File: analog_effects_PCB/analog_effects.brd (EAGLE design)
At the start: 100 x 80 mm, 24 parts, among them J1 575-4, J2 575-4, U1 TL082

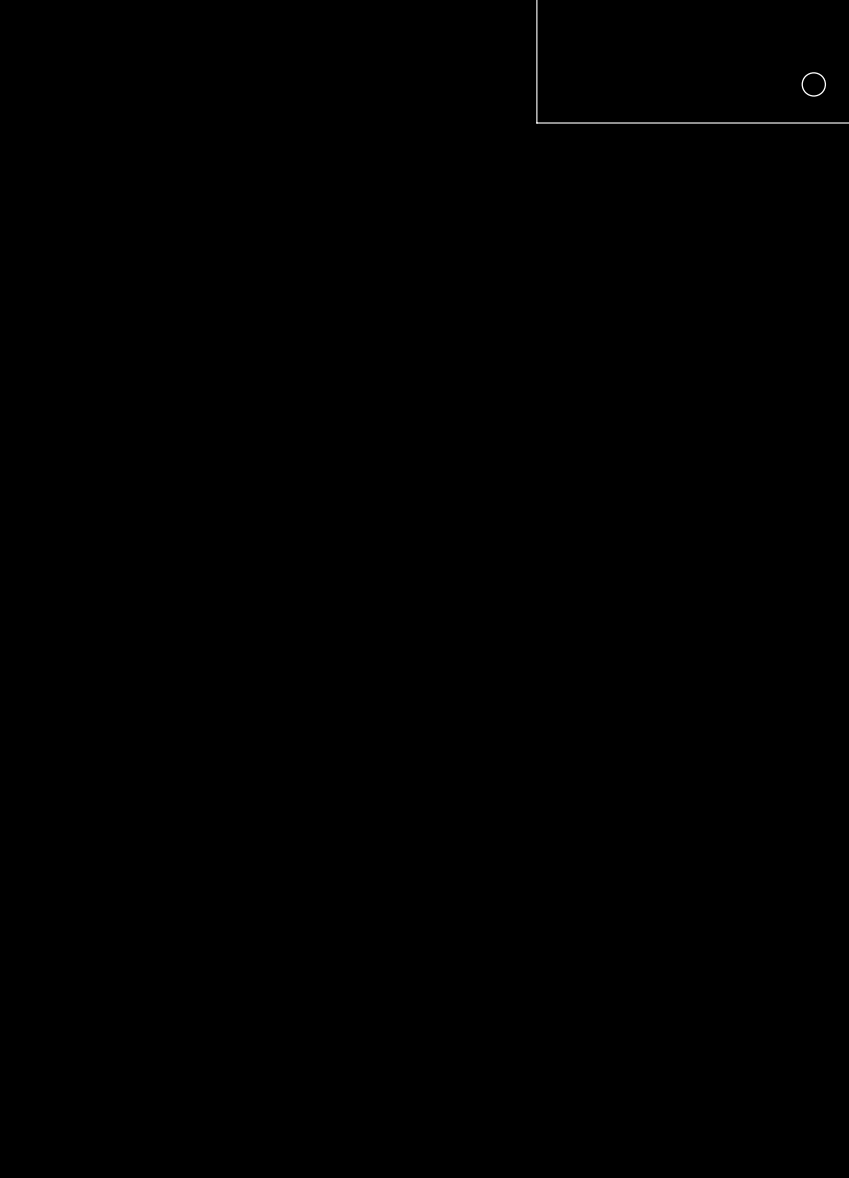
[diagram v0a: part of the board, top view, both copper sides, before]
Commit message: completed the digital pot circuitry on schematic
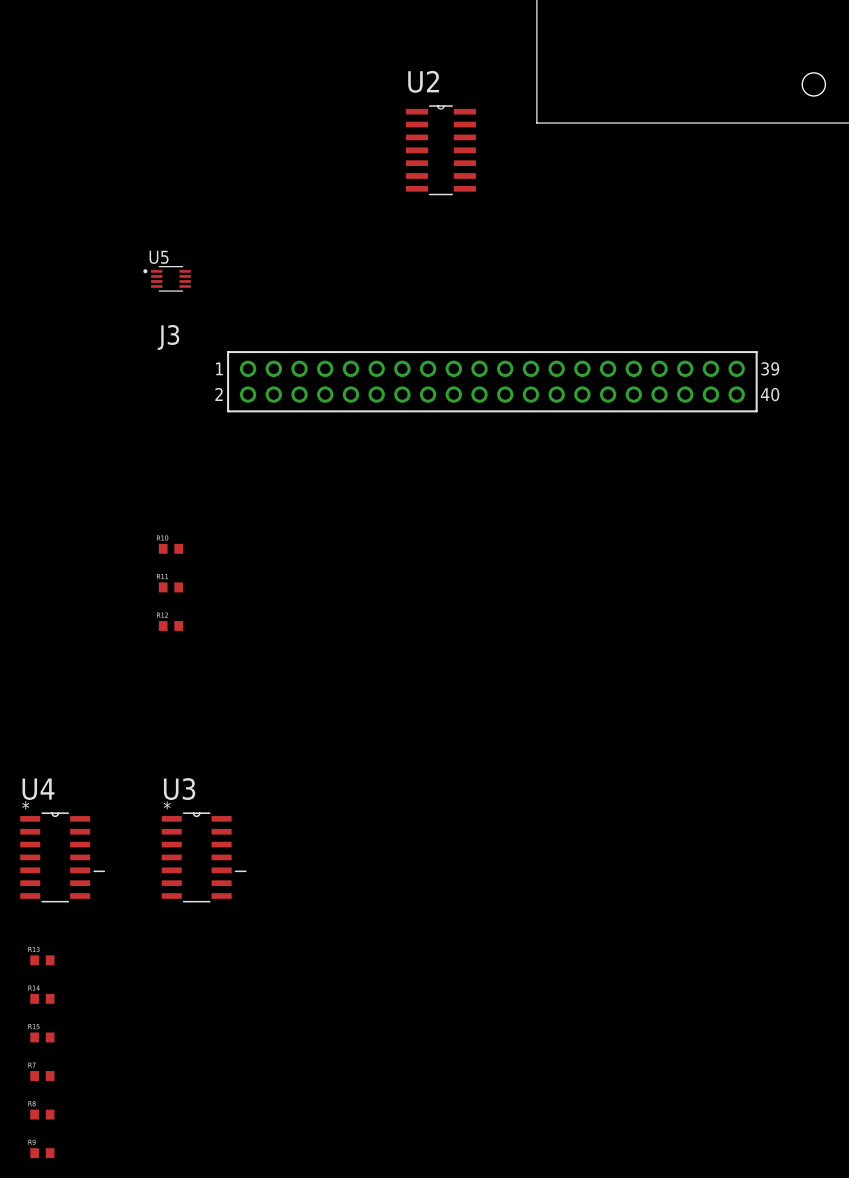
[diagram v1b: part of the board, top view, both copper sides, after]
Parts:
- added J3: SAMTEC-SSQ-120-01-X-DJ, SAMTEC-SSQ-120-01-X-D:SAMTEC-SSQ-120-01-X-D
- added R10, R11, R12, R13, R14, R15, R7, R8, R9: 100kΩ, CRCW0603100KDHEAP:RESC1508X50N
- added U2: AD5241BRZ1M, AD5241BRZ1M:SOIC127P600X175-14N
- added U3: AD5241BRZ10, AD5241BRZ10:SOIC127P600X175-14N
- added U4: AD5241BRZ100, AD5241BRZ100:SOIC127P600X175-14N
- added U5: TS5A3359DCUT, TS5A3359DCUT:SOP50P310X90-8N
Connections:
- new net N$12: R10.1, U2.5
- new net N$13: R3.2, TP6.1, U2.3
- new net N$14: R11.2, U2.7
- new net N$15: R10.2, R11.1, R12.2, U2.4
- new net N$16: C5.2, U3.3
- new net N$17: R12.1, U2.6
- new net N$19: R13.1, U4.7
- new net N$20: R13.2, R14.2, R15.2, U4.4
- new net N$21: R15.1, U4.6
- new net N$22: U3.2, U4.3
- new net N$23: R14.1, U4.5
- new net N$24: R7.1, U3.7
- new net N$25: R7.2, R8.2, R9.2, U3.4
- new net N$26: R9.1, U3.5
- new net N$27: R8.1, U3.6
- new net VCC: U5.8
- net GND: now also U2.10, U2.11, U2.8, U2.9, U3.10, U3.11, U3.8, U3.9, U4.10, U4.11, U4.2, U4.8, U4.9, U5.4; no longer C5.2
- net N$5: now also U2.2; no longer R3.2, TP6.1

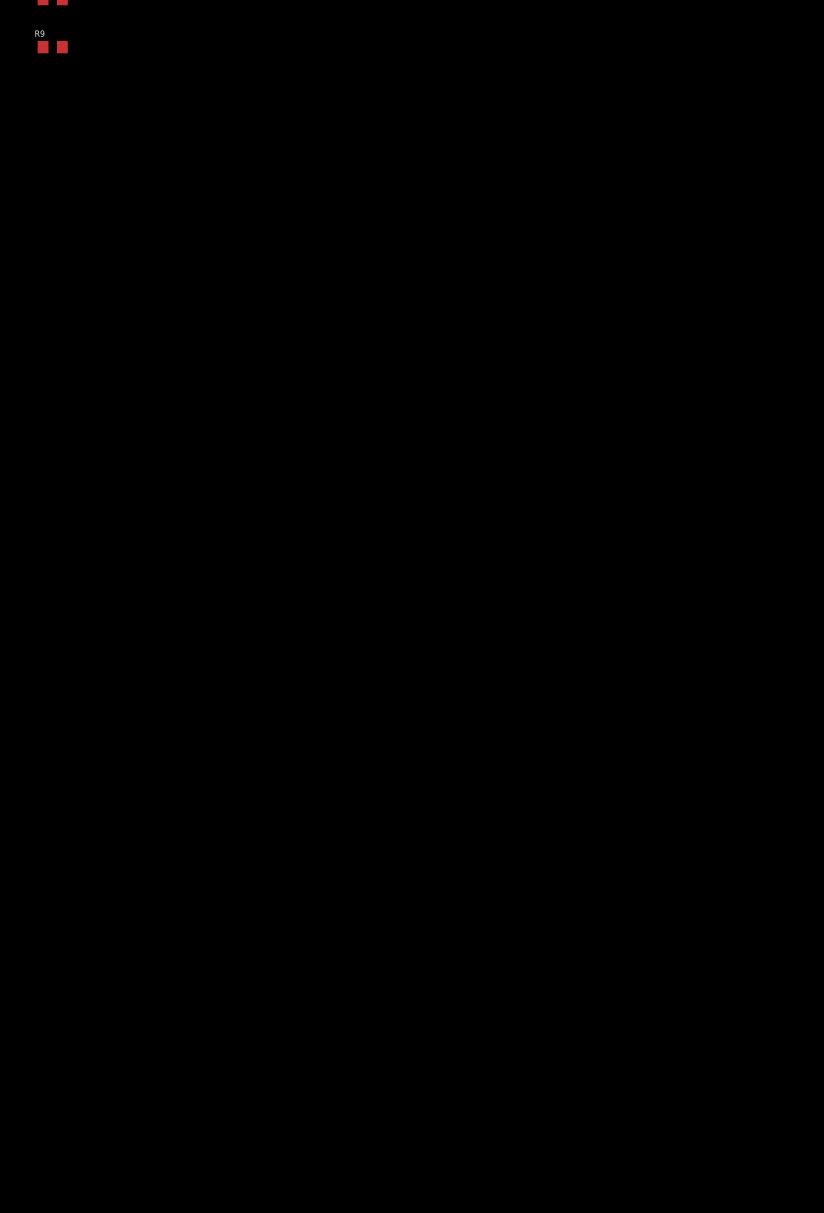
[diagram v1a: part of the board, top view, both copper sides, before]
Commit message: Partly added Fuzz Circuit
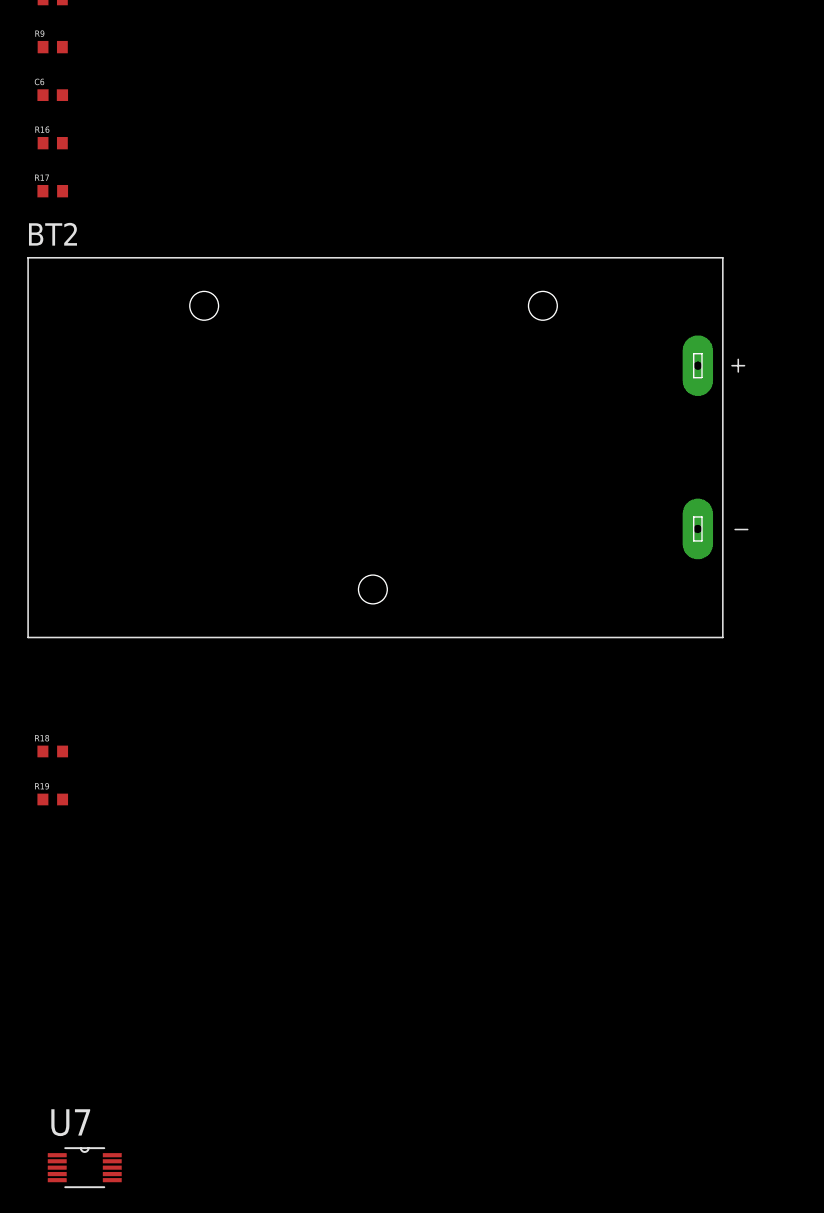
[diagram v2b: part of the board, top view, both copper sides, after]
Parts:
- added BT2: BC9VPC, BC9VPC:BAT_BC9VPC
- added C6: GRM188R6YA225KA12D, GRM188R6YA225KA12D:CAPC1608X90N
- added R16: 100kΩ, CRCW0603100KDHEAP:RESC1508X50N
- added R17: CRCW060333K0JNEAHP, CRCW060333K0JNEAHP:RESC1608X55N
- added R18: CRCW06038K20FKEAC, CRCW06038K20FKEAC:RESC1608X55N
- added R19: CRCW0603470RJNEBC, CRCW0603470RJNEBC:RESC1608X55N
- added U7: AD5258BRMZ1-R7, AD5258BRMZ1-R7:SOP50P490X110-10N
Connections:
- new net FUZZ_IN: C6.1
- new net N$10: R17.1
- new net N$11: BT2.N, R17.2, R19.2
- new net N$18: R18.1, R19.1
- new net N$28: R16.2
- new net N$9: C6.2, R16.1
- new net VDD: U7.8
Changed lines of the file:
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@@
 <layer number="97" name="Info" color="7" fill="1" visible="no" active="no"/>
 <layer number="98" name="Guide" color="6" fill="1" visible="no" active="no"/>
+<layer number="99" name="SpiceOrder" color="7" fill="1" visible="no" active="no"/>
 </layers>
 <board>
@@
 <attribute name="VALUE" x="-123.36" y="-94.8" size="0.5" layer="27" align="top-left"/>
 </element>
+<element name="C6" library="GRM188R6YA225KA12D" package="CAPC1608X90N" value="GRM188R6YA225KA12D" x="-121.92" y="-97.79" smashed="yes">
+<attribute name="AVAILABILITY" value="Warning" x="-121.92" y="-97.79" size="1.778" layer="27" display="off"/>
+<attribute name="DESCRIPTION" value=" SMD capacitor X5R(EIA) with capacitance 2.2uF Tol.10%. Rated voltage 35Vdc 85C " x="-121.92" y="-97.79" size="1.778" layer="27" display="off"/>
+<attribute name="MF" value="Murata" x="-121.92" y="-97.79" size="1.778" layer="27" display="off"/>
+<attribute name="MP" value="GRM188R6YA225KA12D" x="-121.92" y="-97.79" size="1.778" layer="27" display="off"/>
+<attribute name="NAME" x="-123.38" y="-96.99" size="0.5" layer="25"/>
+<attribute name="PACKAGE" value="1608 Murata" x="-121.92" y="-97.79" size="1.778" layer="27" display="off"/>
+<attribute name="PRICE" value="None" x="-121.92" y="-97.79" size="1.778" layer="27" display="off"/>
+<attribute name="PURCHASE-URL" value="https://pricing.snapeda.com/search/part/GRM188R6YA225KA12D/?ref=eda" x="-121.92" y="-97.79" size="1.778" layer="27" display="off"/>
+<attribute name="VALUE" x="-123.38" y="-98.59" size="0.5" layer="27" align="top-left"/>
+</element>
+<element name="R16" library="CRCW0603100KDHEAP" package="RESC1508X50N" value="100kΩ" x="-121.92" y="-101.6" smashed="yes">
+<attribute name="AVAILABILITY" value="Good" x="-121.92" y="-101.6" size="1.778" layer="27" display="off"/>
+<attribute name="DESCRIPTION" value=" Res Thick Film 0603 100K Ohm 0.5% 0.1W(1/10W) ±50ppm/C Pad SMD Automotive T/R " x="-121.92" y="-101.6" size="1.778" layer="27" display="off"/>
+<attribute name="MF" value="Vishay Dale" x="-121.92" y="-101.6" size="1.778" layer="27" display="off"/>
+<attribute name="MP" value="CRCW0603100KDHEAP" x="-121.92" y="-101.6" size="1.778" layer="27" display="off"/>
+<attribute name="NAME" x="-123.36" y="-100.78" size="0.5" layer="25"/>
+<attribute name="PACKAGE" value="1508 Vishay" x="-121.92" y="-101.6" size="1.778" layer="27" display="off"/>
+<attribute name="PRICE" value="None" x="-121.92" y="-101.6" size="1.778" layer="27" display="off"/>
+<attribute name="PURCHASE-URL" value="https://pricing.snapeda.com/search/part/CRCW0603100KDHEAP/?ref=eda" x="-121.92" y="-101.6" size="1.778" layer="27" display="off"/>
+<attribute name="VALUE" x="-123.36" y="-102.42" size="0.5" layer="27" align="top-left"/>
+</element>
+<element name="R17" library="CRCW060333K0JNEAHP" package="RESC1608X55N" value="CRCW060333K0JNEAHP" x="-121.92" y="-105.41" smashed="yes">
+<attribute name="AVAILABILITY" value="Warning" x="-121.92" y="-105.41" size="1.778" layer="27" display="off"/>
+<attribute name="DESCRIPTION" value=" RES SMD 33K OHM 5% 1/4W 0603 " x="-121.92" y="-105.41" size="1.778" layer="27" display="off"/>
+<attribute name="MF" value="Vishay" x="-121.92" y="-105.41" size="1.778" layer="27" display="off"/>
+<attribute name="MP" value="CRCW060333K0JNEAHP" x="-121.92" y="-105.41" size="1.778" layer="27" display="off"/>
+<attribute name="NAME" x="-123.38" y="-104.59" size="0.5" layer="25"/>
+<attribute name="PACKAGE" value="1608 Vishay" x="-121.92" y="-105.41" size="1.778" layer="27" display="off"/>
+<attribute name="PRICE" value="None" x="-121.92" y="-105.41" size="1.778" layer="27" display="off"/>
+<attribute name="PURCHASE-URL" value="https://pricing.snapeda.com/search/part/CRCW060333K0JNEAHP/?ref=eda" x="-121.92" y="-105.41" size="1.778" layer="27" display="off"/>
+<attribute name="VALUE" x="-123.38" y="-106.23" size="0.5" layer="27" align="top-left"/>
+</element>
+<element name="BT2" library="BC9VPC" package="BAT_BC9VPC" value="BC9VPC" x="-96.52" y="-125.73" smashed="yes">
+<attribute name="DESCRIPTION" value=" BATTERY HOLDER 9V PC PIN " x="-96.52" y="-125.73" size="1.778" layer="27" display="off"/>
+<attribute name="DIGI-KEY_PART_NUMBER" value="BC9VPC-ND" x="-96.52" y="-125.73" size="1.778" layer="27" display="off"/>
+<attribute name="MF" value="MPD" x="-96.52" y="-125.73" size="1.778" layer="27" display="off"/>
+<attribute name="MP" value="BC9VPC" x="-96.52" y="-125.73" size="1.778" layer="27" display="off"/>
+<attribute name="NAME" x="-124.02" y="-109.73" size="1.778" layer="25"/>
+<attribute name="PACKAGE" value="None" x="-96.52" y="-125.73" size="1.778" layer="27" display="off"/>
+<attribute name="PURCHASE-URL" value="https://pricing.snapeda.com/search/part/BC9VPC/?ref=eda" x="-96.52" y="-125.73" size="1.778" layer="27" display="off"/>
+<attribute name="VALUE" x="-124.02" y="-143.23" size="1.778" layer="27"/>
+</element>
+<element name="R18" library="CRCW06038K20FKEAC" package="RESC1608X55N" value="CRCW06038K20FKEAC" x="-121.92" y="-149.86" smashed="yes">
+<attribute name="AVAILABILITY" value="Warning" x="-121.92" y="-149.86" size="1.778" layer="27" display="off"/>
+<attribute name="DESCRIPTION" value=" Res Thick Film 0603 8.2K Ohm 1% 0.1W(1/10W) ±100ppm/°C Pad SMD T/R " x="-121.92" y="-149.86" size="1.778" layer="27" display="off"/>
+<attribute name="MF" value="Vishay" x="-121.92" y="-149.86" size="1.778" layer="27" display="off"/>
+<attribute name="MP" value="CRCW06038K20FKEAC" x="-121.92" y="-149.86" size="1.778" layer="27" display="off"/>
+<attribute name="NAME" x="-123.38" y="-149.06" size="0.5" layer="25"/>
+<attribute name="PACKAGE" value="1608 Rohm Semiconductor" x="-121.92" y="-149.86" size="1.778" layer="27" display="off"/>
+<attribute name="PRICE" value="None" x="-121.92" y="-149.86" size="1.778" layer="27" display="off"/>
+<attribute name="PURCHASE-URL" value="https://pricing.snapeda.com/search/part/CRCW06038K20FKEAC/?ref=eda" x="-121.92" y="-149.86" size="1.778" layer="27" display="off"/>
+<attribute name="VALUE" x="-123.38" y="-150.66" size="0.5" layer="27" align="top-left"/>
+</element>
+<element name="R19" library="CRCW0603470RJNEBC" package="RESC1608X55N" value="CRCW0603470RJNEBC" x="-121.92" y="-153.67" smashed="yes">
+<attribute name="AVAILABILITY" value="Good" x="-121.92" y="-153.67" size="1.778" layer="27" display="off"/>
+<attribute name="DESCRIPTION" value=" 470 Ohms ±5% 0.1W, 1/10W Chip Resistor 0603 (1608 Metric) Thick Film " x="-121.92" y="-153.67" size="1.778" layer="27" display="off"/>
+<attribute name="MF" value="Vishay" x="-121.92" y="-153.67" size="1.778" layer="27" display="off"/>
+<attribute name="MP" value="CRCW0603470RJNEBC" x="-121.92" y="-153.67" size="1.778" layer="27" display="off"/>
+<attribute name="NAME" x="-123.38" y="-152.87" size="0.5" layer="25"/>
+<attribute name="PACKAGE" value="1608 Rohm Semiconductor" x="-121.92" y="-153.67" size="1.778" layer="27" display="off"/>
+<attribute name="PRICE" value="None" x="-121.92" y="-153.67" size="1.778" layer="27" display="off"/>
+<attribute name="PURCHASE-URL" value="https://pricing.snapeda.com/search/part/CRCW0603470RJNEBC/?ref=eda" x="-121.92" y="-153.67" size="1.778" layer="27" display="off"/>
+<attribute name="VALUE" x="-123.38" y="-154.47" size="0.5" layer="27" align="top-left"/>
+</element>
+<element name="U7" library="AD5258BRMZ1-R7" package="SOP50P490X110-10N" value="AD5258BRMZ1-R7" x="-119.38" y="-182.88" smashed="yes">
+<attribute name="AVAILABILITY" value="Good" x="-119.38" y="-182.88" size="1.778" layer="27" display="off"/>
+<attribute name="DESCRIPTION" value=" Digital Potentiometer 1k Ohm 1 Circuit 64 Taps I²C Interface 10-MSOP " x="-119.38" y="-182.88" size="1.778" layer="27" display="off"/>
+<attribute name="MF" value="Analog Devices Inc." x="-119.38" y="-182.88" size="1.778" layer="27" display="off"/>
+<attribute name="MP" value="AD5258BRMZ1-R7" x="-119.38" y="-182.88" size="1.778" layer="27" display="off"/>
+<attribute name="NAME" x="-122.257459375" y="-180.33358125" size="2.08806875" layer="25" ratio="10" rot="SR0"/>
+<attribute name="PACKAGE" value="None" x="-119.38" y="-182.88" size="1.778" layer="27" display="off"/>
+<attribute name="PRICE" value="None" x="-119.38" y="-182.88" size="1.778" layer="27" display="off"/>
+<attribute name="PURCHASE-URL" value="https://pricing.snapeda.com/search/part/AD5258BRMZ1-R7/?ref=eda" x="-119.38" y="-182.88" size="1.778" layer="27" display="off"/>
+<attribute name="VALUE" x="-122.84063125" y="-187.33301875" size="2.086559375" layer="27" ratio="10" rot="SR0"/>
+</element>
 </elements>
 <signals>
@@
 <wire x1="-109.1438" y1="-67.31" x2="-122.685" y2="-90.17" width="0" layer="19" extent="1-1"/>
 </signal>
+<signal name="FUZZ_IN">
+<contactref element="C6" pad="1"/>
+</signal>
+<signal name="N$9">
+<contactref element="C6" pad="2"/>
+<contactref element="R16" pad="1"/>
+<wire x1="-121.15" y1="-97.79" x2="-122.685" y2="-101.6" width="0" layer="19" extent="1-1"/>
+</signal>
+<signal name="N$10">
+<contactref element="R17" pad="1"/>
+</signal>
+<signal name="N$11">
+<contactref element="R17" pad="2"/>
+<contactref element="BT2" pad="N"/>
+<contactref element="R19" pad="2"/>
+<wire x1="-121.14" y1="-153.67" x2="-121.14" y2="-105.41" width="0" layer="19" extent="1-1"/>
+<wire x1="-70.739" y1="-132.207" x2="-121.14" y2="-153.67" width="0" layer="19" extent="1-1"/>
+</signal>
+<signal name="N$18">
+<contactref element="R19" pad="1"/>
+<contactref element="R18" pad="1"/>
+<wire x1="-122.7" y1="-149.86" x2="-122.7" y2="-153.67" width="0" layer="19" extent="1-1"/>
+</signal>
+<signal name="N$28">
+<contactref element="R16" pad="2"/>
+</signal>
+<signal name="VDD">
+<contactref element="U7" pad="8"/>
+</signal>
 </signals>
